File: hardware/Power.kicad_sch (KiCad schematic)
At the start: 33 parts, among them J1 JST XH, J2 JST XH, J22 JST XH, J23 JST XH, J24 JST XH, J25 JST XH, J26 JST XH, J27 JST XH, Q1 NCE40P40K, U4 AMS1117-3.3, U5 DCBuck

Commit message: Update PrntrBoard fabrication files.
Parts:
- U5: now left out of the parts list

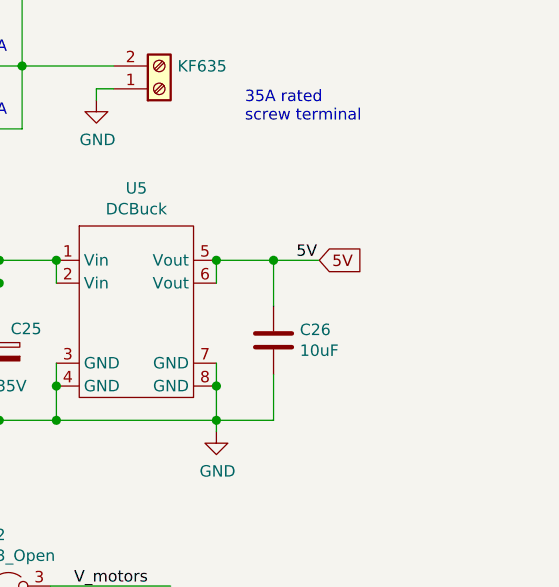
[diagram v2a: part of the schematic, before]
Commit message: 5V terminal added
- dedicated input of 5V  to allow control of external 24V supply
- minotr tracks adjustment / cleaning
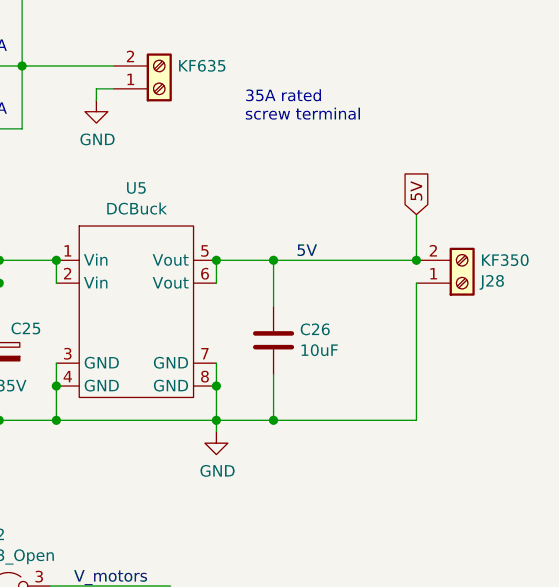
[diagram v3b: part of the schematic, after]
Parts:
- added J28: KF350, PrntrBoardV2:TerminalBlock_Phoenix_PT-1,5-2-3.5-H_1x02_P3.50mm_Horizontal, symbol Connector:Screw_Terminal_01x02
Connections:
- net 5V: now also J28.2 (Pin_2)
- net GND: now also J28.1 (Pin_1)
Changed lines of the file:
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@@
   (junction (at 158.115 87.63) (diameter 1.016) (color 0 0 0 0))
   (junction (at 164.465 69.85) (diameter 1.016) (color 0 0 0 0))
+  (junction (at 164.465 87.63) (diameter 1.016) (color 0 0 0 0))
+  (junction (at 180.34 69.85) (diameter 1.016) (color 0 0 0 0))
   (wire (pts (xy 35.56 122.555) (xy 44.45 122.555))
     (stroke (width 0) (type solid) (color 0 0 0 0))
@@
     (stroke (width 0) (type solid) (color 0 0 0 0))
   )
-  (wire (pts (xy 164.465 69.85) (xy 169.545 69.85))
+  (wire (pts (xy 164.465 69.85) (xy 180.34 69.85))
     (stroke (width 0) (type solid) (color 0 0 0 0))
   )
@@
   )
   (wire (pts (xy 164.465 87.63) (xy 158.115 87.63))
+    (stroke (width 0) (type solid) (color 0 0 0 0))
+  )
+  (wire (pts (xy 180.34 64.77) (xy 180.34 69.85))
+    (stroke (width 0) (type solid) (color 0 0 0 0))
+  )
+  (wire (pts (xy 180.34 72.39) (xy 180.34 87.63))
+    (stroke (width 0) (type solid) (color 0 0 0 0))
+  )
+  (wire (pts (xy 180.34 87.63) (xy 164.465 87.63))
     (stroke (width 0) (type solid) (color 0 0 0 0))
   )
@@
     (effects (font (size 1.27 1.27)) (justify right))
   )
-  (global_label "5V" (shape input) (at 169.545 69.85 0)    (property "Intersheet References" "${INTERSHEET_REFS}" (id 0) (at 0 0 0)
+  (global_label "5V" (shape input) (at 180.34 64.77 90)    (property "Intersheet References" "${INTERSHEET_REFS}" (id 0) (at 110.49 234.315 0)
       (effects (font (size 1.27 1.27)) hide)
     )
@@
       (effects (font (size 1.27 1.27)) hide)
     )
+  )
+  (symbol (lib_id "Connector:Screw_Terminal_01x02") (at 185.42 72.39 0) (mirror x) (unit 1)
+    (in_bom yes) (on_board yes)
+    (property "Reference" "J28" (id 0) (at 187.452 72.1868 0)
+      (effects (font (size 1.27 1.27)) (justify left))
+    )
+    (property "Value" "KF350" (id 1) (at 187.452 69.8754 0)
+      (effects (font (size 1.27 1.27)) (justify left))
+    )
+    (property "Footprint" "PrntrBoardV2:TerminalBlock_Phoenix_PT-1,5-2-3.5-H_1x02_P3.50mm_Horizontal" (id 2) (at 185.42 72.39 0)
+      (effects (font (size 1.27 1.27)) hide)
+    )
+    (property "Datasheet" "~" (id 3) (at 185.42 72.39 0)
+      (effects (font (size 1.27 1.27)) hide)
+    )

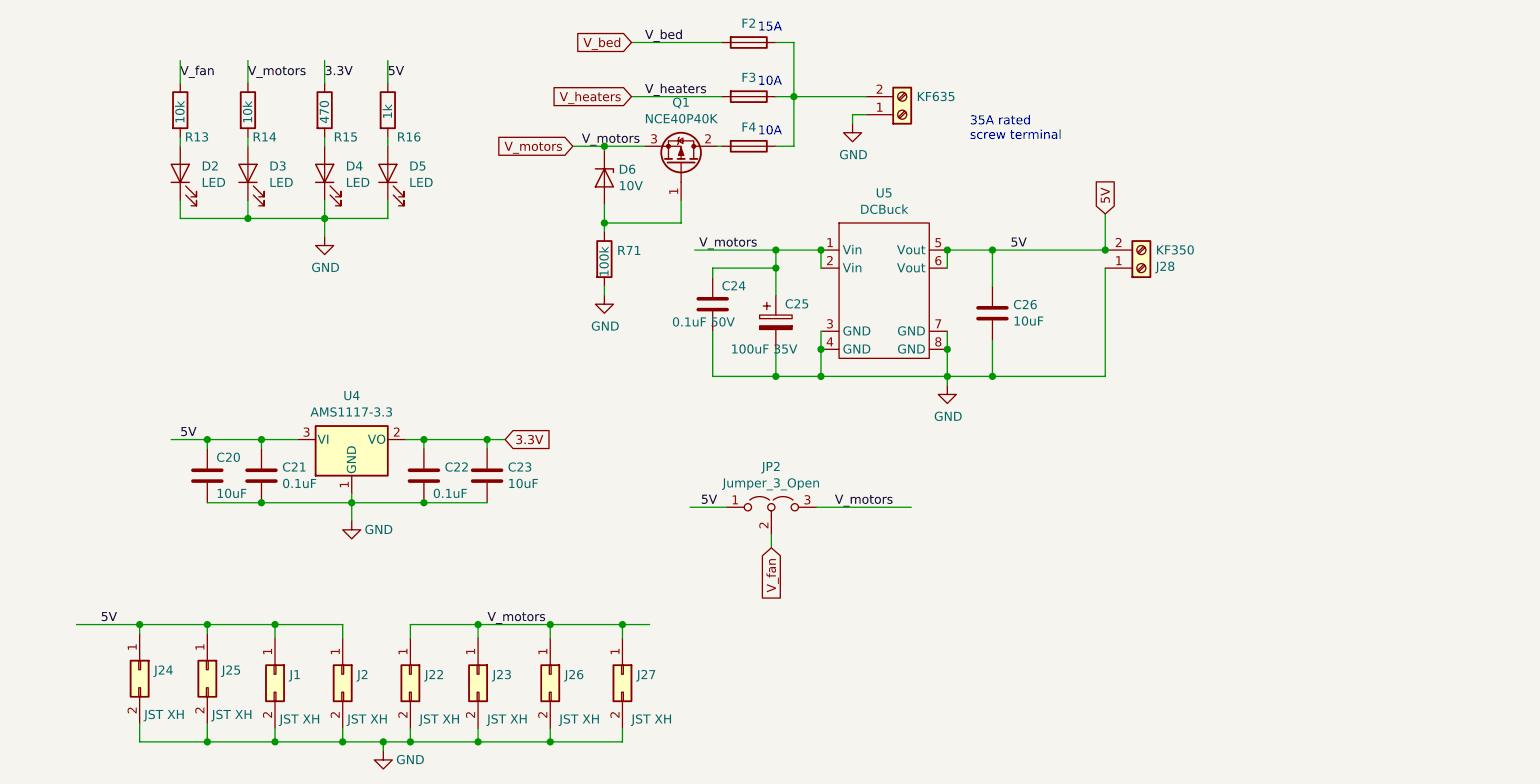
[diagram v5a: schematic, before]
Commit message: Added separate power supply for motor drivers, to accomodate high voltage driver versions.
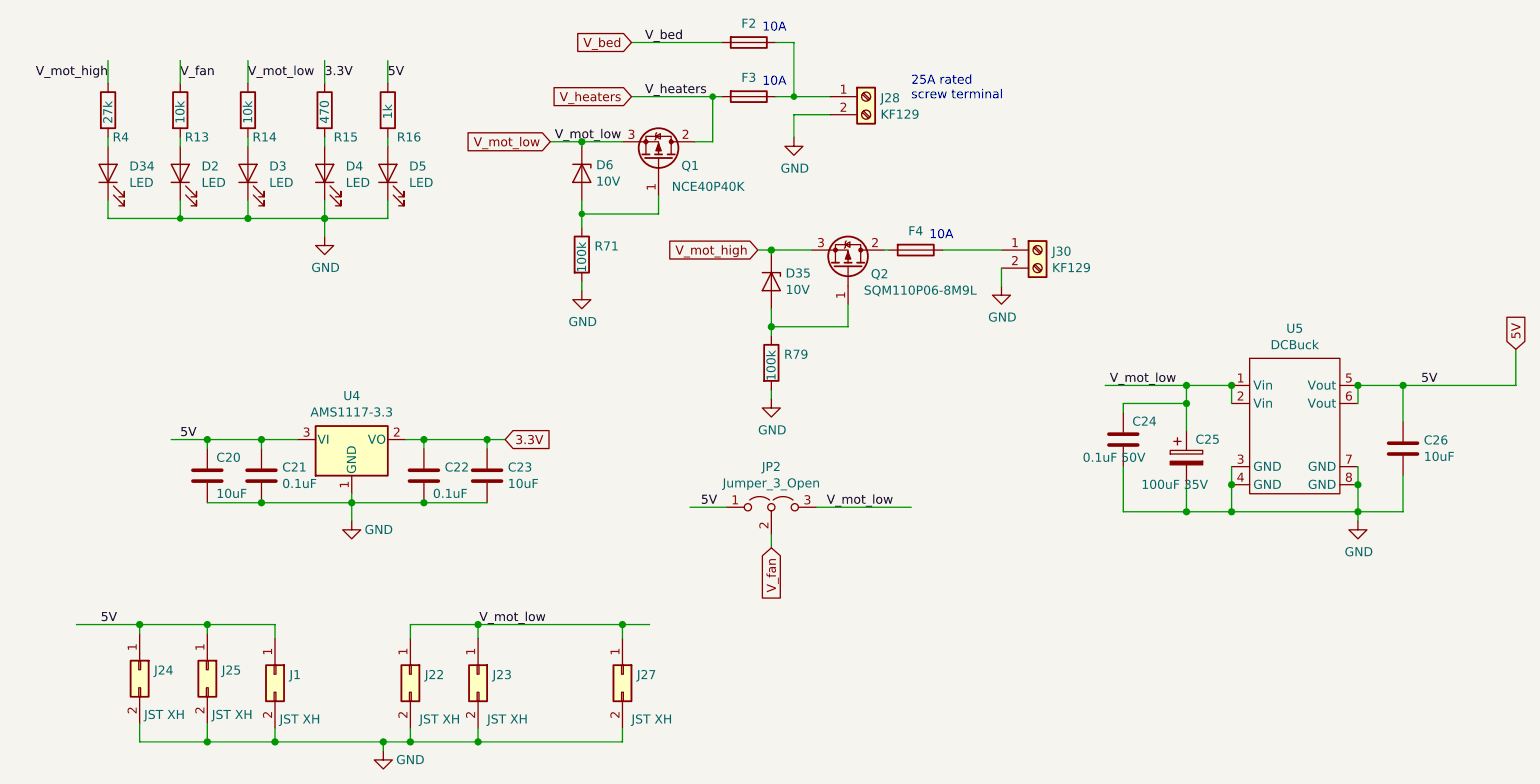
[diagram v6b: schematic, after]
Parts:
- removed J2, J26: JST XH, Connector_JST:JST_XH_B2B-XH-A_1x02_P2.50mm_Vertical, symbol Connector_Generic:Conn_02x01
- removed J_power_in1: KF635, TerminalBlock_MetzConnect:TerminalBlock_MetzConnect_Type701_RT11L02HGLU_1x02_P6.35mm_Horizontal, symbol Connector:Screw_Terminal_01x02
- added D34: LED, PrntrBoardV2:LED_0603_1608Metric, symbol Device:LED
- added D35: 10V, Diode_SMD:D_SOD-323, symbol Device:D_Zener
- added J30: KF129, PrntrBoardV2:TerminalBlock_Phoenix_MKDS-1,5-2-5.08_1x02_P5.08mm_Horizontal, symbol Connector:Screw_Terminal_01x02
- added Q2: SQM110P06-8M9L, Package_TO_SOT_SMD:TO-252-2, symbol Transistor_FET:IRF4905
- added R4: 27k, PrntrBoardV2:R_0603_1608Metric, symbol Device:R
- added R79: 100k, PrntrBoardV2:R_0603_1608Metric, symbol Device:R
- J28: value KF350 -> KF129; footprint PrntrBoardV2:TerminalBlock_Phoenix_PT-1,5-2-3.5-H_1x02_P3.50mm_Horizontal -> PrntrBoardV2:TerminalBlock_Phoenix_MKDS-1,5-2-5.08_1x02_P5.08mm_Horizontal
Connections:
- net 5V: no longer J28.2 (Pin_2)
- net GND: now also J28.2 (Pin_2), D34.1 (K), J30.2 (Pin_2), R79.2; no longer J28.1 (Pin_1)
- net V_heaters: now also Q1.2 (D)
- net at F2.1, F3.1: now also J28.1 (Pin_1); no longer F4.1
- net at F4.2: now also Q2.2 (D); no longer Q1.2 (D)
- net V_motors renamed V_mot_low
- new net: F4.1, J30.1 (Pin_1)
- new net: D34.2 (A), R4.2
- new net: D35.2 (A), Q2.1 (G), R79.1
- new net V_mot_high: D35.1 (K), Q2.3 (S), R4.1
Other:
- note added: "25A rated screw terminal"
- note removed: "15A"
- note removed: "35A rated screw terminal"
- moved on the sheet: C24, C25, C26, D6, Q1, R71, U5

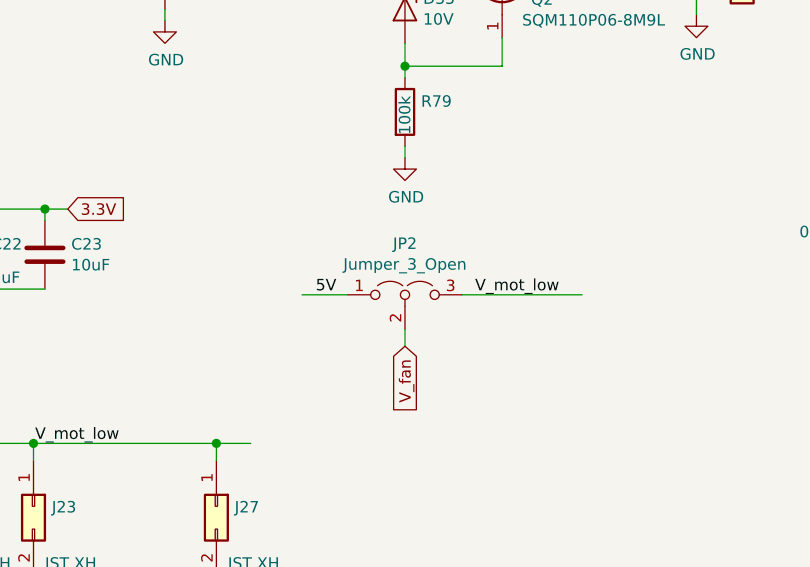
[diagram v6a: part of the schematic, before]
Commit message: Add voltage selection for each stepper driver.
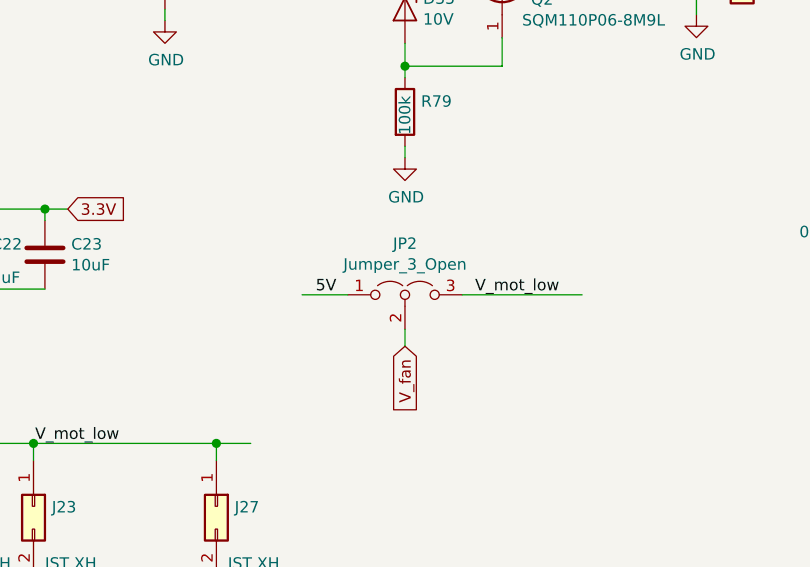
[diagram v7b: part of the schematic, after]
